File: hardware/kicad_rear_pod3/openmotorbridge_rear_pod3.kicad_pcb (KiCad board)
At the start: 4 copper layers, 50 x 35 mm, 25 parts, among them J1 M8_3PIN_SOCKET, U1 ESP32-C3-WROOM-02, U2 MAX-M10S, U3 SX1262

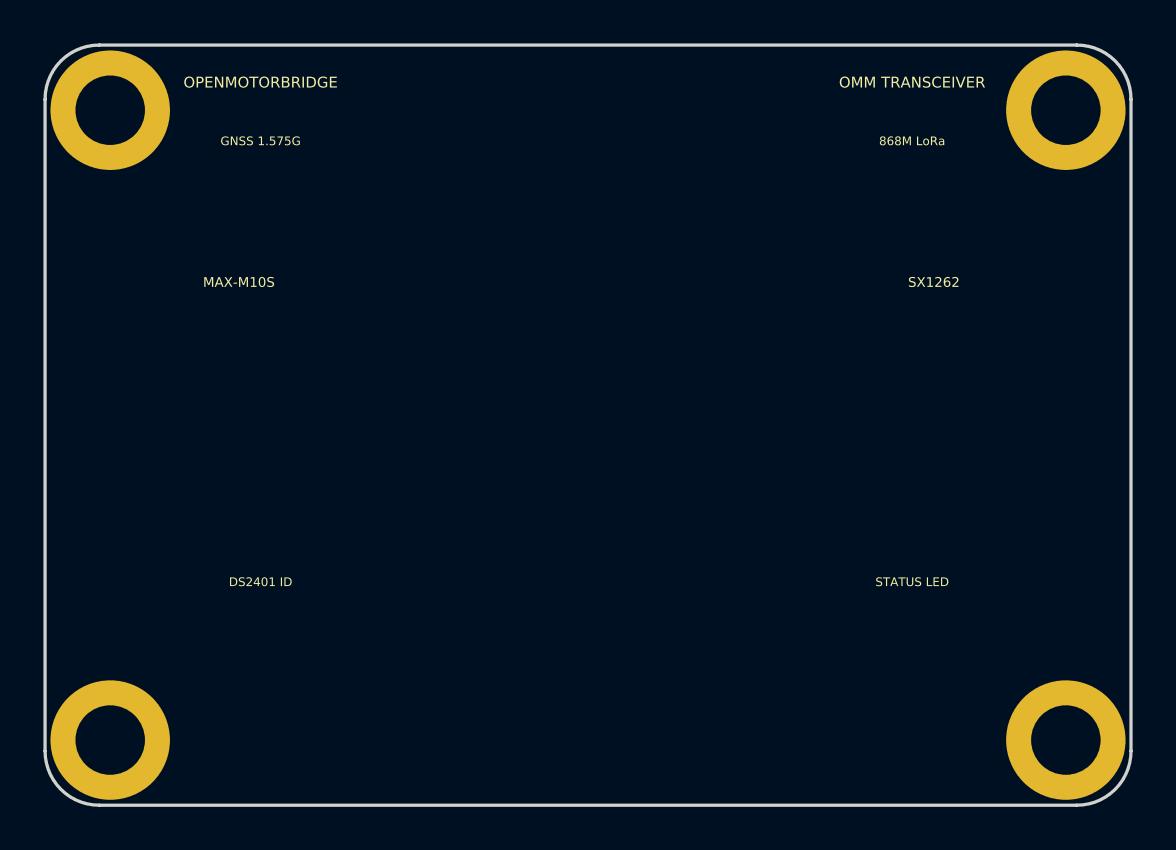
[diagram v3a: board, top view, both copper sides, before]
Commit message: fix(hardware): shift ESP32-C3 module to Y=90.0 on Rear Pod 3 to ensure 2.5mm margin inside PCB outline with zero overhang
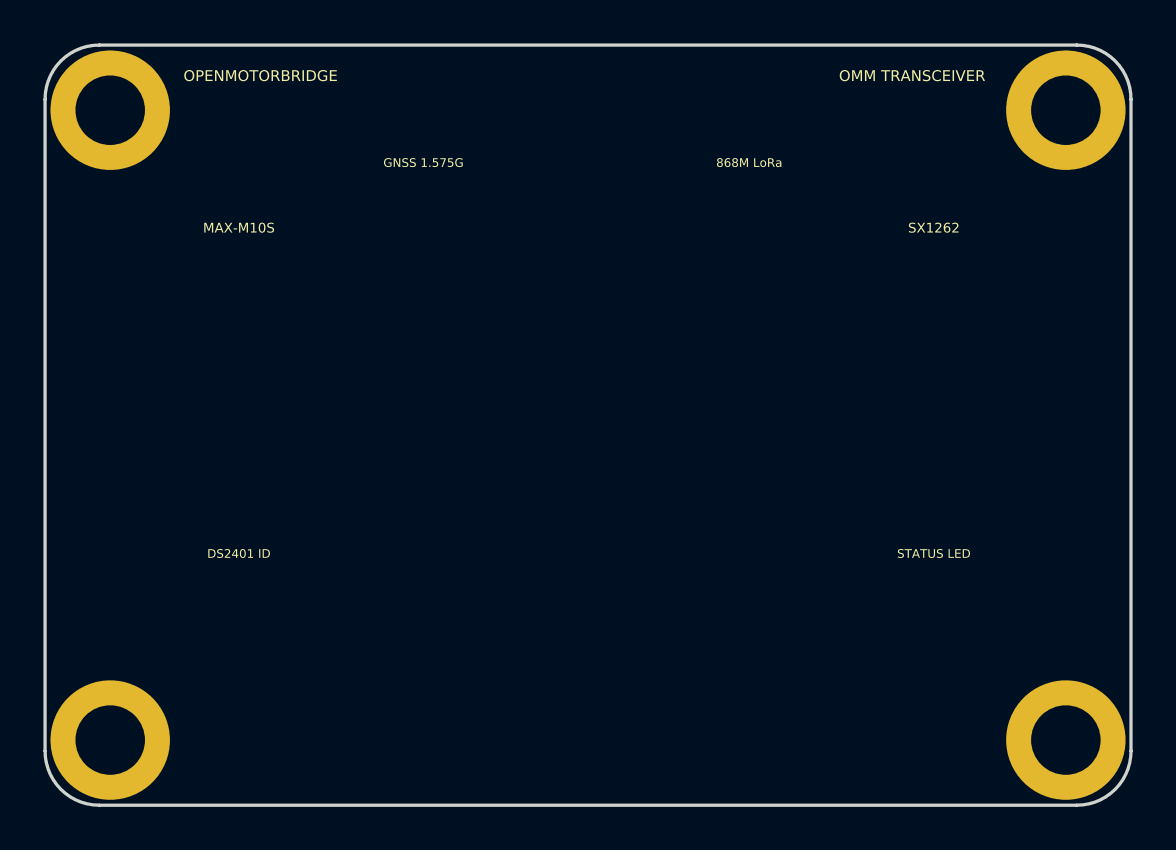
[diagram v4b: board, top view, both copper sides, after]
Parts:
- moved U1 4.00 mm to (125.0, 90.0)
- moved U2 3.00 mm to (109.0, 83.0)
- moved U3 3.00 mm to (141.0, 83.0)
- moved C3 1.50 mm to (109.0, 90.0)
- moved C4 1.50 mm to (145.5, 90.0)
- moved J1 1.50 mm to (125.0, 102.0)
- moved L1 1.50 mm to (141.0, 90.0)
- moved D1 1.41 mm to (141.0, 97.0)
- moved U4 1.41 mm to (109.0, 97.0)
- moved ANT1 1.00 mm to (142.0, 75.0)
- moved ANT2 1.00 mm to (108.0, 75.0)
- moved C1 0.50 mm to (113.5, 93.0)
- moved C2 0.50 mm to (136.5, 93.0)
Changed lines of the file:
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@@
 	(footprint "RF_Module:ESP32-C3-WROOM-02"
 		(layer "F.Cu")
-		(at 125 86)
+		(at 125 90)
 		(property "Reference" "U1"
 			(at 0 -8 0)
@@
 	(footprint ""
 		(layer "F.Cu")
-		(at 141 91.5)
+		(at 141 90)
 		(property "Reference" "L1"
 			(at 0 0 0)
@@
 	(footprint ""
 		(layer "F.Cu")
-		(at 142 76)
+		(at 142 75)
 		(property "Reference" "ANT1"
 			(at 0 0 0)
@@
 	(footprint ""
 		(layer "F.Cu")
-		(at 109 91.5)
+		(at 109 90)
 		(property "Reference" "C3"
 			(at 0 0 0)
@@
 	(footprint "RF_GPS:u-blox_MAX-M10S"
 		(layer "F.Cu")
-		(at 109 86)
+		(at 109 83)
 		(property "Reference" "U2"
 			(at 0 -6 0)
@@
 	(footprint ""
 		(layer "F.Cu")
-		(at 136.5 92.5)
+		(at 136.5 93)
 		(property "Reference" "C2"
 			(at 0 0 0)
@@
 	(footprint ""
 		(layer "F.Cu")
-		(at 110 98)
+		(at 109 97)
 		(property "Reference" "U4"
 			(at 0 0 0)
@@
 	(footprint ""
 		(layer "F.Cu")
-		(at 108 76)
+		(at 108 75)
 		(property "Reference" "ANT2"
 			(at 0 0 0)
@@
 	(footprint ""
 		(layer "F.Cu")
-		(at 140 98)
+		(at 141 97)
 		(property "Reference" "D1"
 			(at 0 0 0)
@@
 	(footprint ""
 		(layer "F.Cu")
-		(at 113.5 92.5)
+		(at 113.5 93)
 		(property "Reference" "C1"
 			(at 0 0 0)
@@
 	(footprint "Package_DFN_QFN:QFN-24-1EP_4x4mm_P0.5mm_EP2.6x2.6mm"
 		(layer "F.Cu")
-		(at 141 86)
+		(at 141 83)
 		(property "Reference" "U3"
 			(at 0 -3.2 0)
@@
 	(footprint ""
 		(layer "F.Cu")
-		(at 145.5 91.5)
+		(at 145.5 90)
 		(property "Reference" "C4"
 			(at 0 0 0)
@@
 	(footprint "Connector_PinHeader_2.54mm:PinHeader_1x03_P2.54mm_Vertical"
 		(layer "B.Cu")
-		(at 125 100.5 90)
+		(at 125 102 90)
 		(property "Reference" "J1"
 			(at 0 -2.5 90)
@@
 		(layer "Edge.Cuts")
 	)
-	(gr_text "GNSS 1.575G"
-		(at 110 74.5 0)
+	(gr_text "DS2401 ID"
+		(at 109 93.5 0)
 		(layer "F.SilkS")
 		(effects
@@
 		)
 	)
-	(gr_text "DS2401 ID"
-		(at 110 94.8 0)
+	(gr_text "GNSS 1.575G"
+		(at 117.5 75.5 0)
 		(layer "F.SilkS")
 		(effects
@@
 	)
 	(gr_text "868M LoRa"
-		(at 140 74.5 0)
+		(at 132.5 75.5 0)
 		(layer "F.SilkS")
 		(effects
@@
 	)
 	(gr_text "STATUS LED"
-		(at 140 94.8 0)
+		(at 141 93.5 0)
 		(layer "F.SilkS")
 		(effects
@@
 	)
 	(gr_text "MAX-M10S"
-		(at 109 81 0)
+		(at 109 78.5 0)
 		(layer "F.SilkS")
 		(effects
@@
 	)
 	(gr_text "SX1262"
-		(at 141 81 0)
+		(at 141 78.5 0)
 		(layer "F.SilkS")
 		(effects
@@
 	)
 	(gr_text "OPENMOTORBRIDGE"
-		(at 110 71.8 0)
+		(at 110 71.5 0)
 		(layer "F.SilkS")
 		(effects
@@
 	)
 	(gr_text "OMM TRANSCEIVER"
-		(at 140 71.8 0)
+		(at 140 71.5 0)
 		(layer "F.SilkS")
 		(effects

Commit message: feat(hardware): implement flat OMM PCB with horizontal front-edge mating, 500mA PTC fuse, and status LED
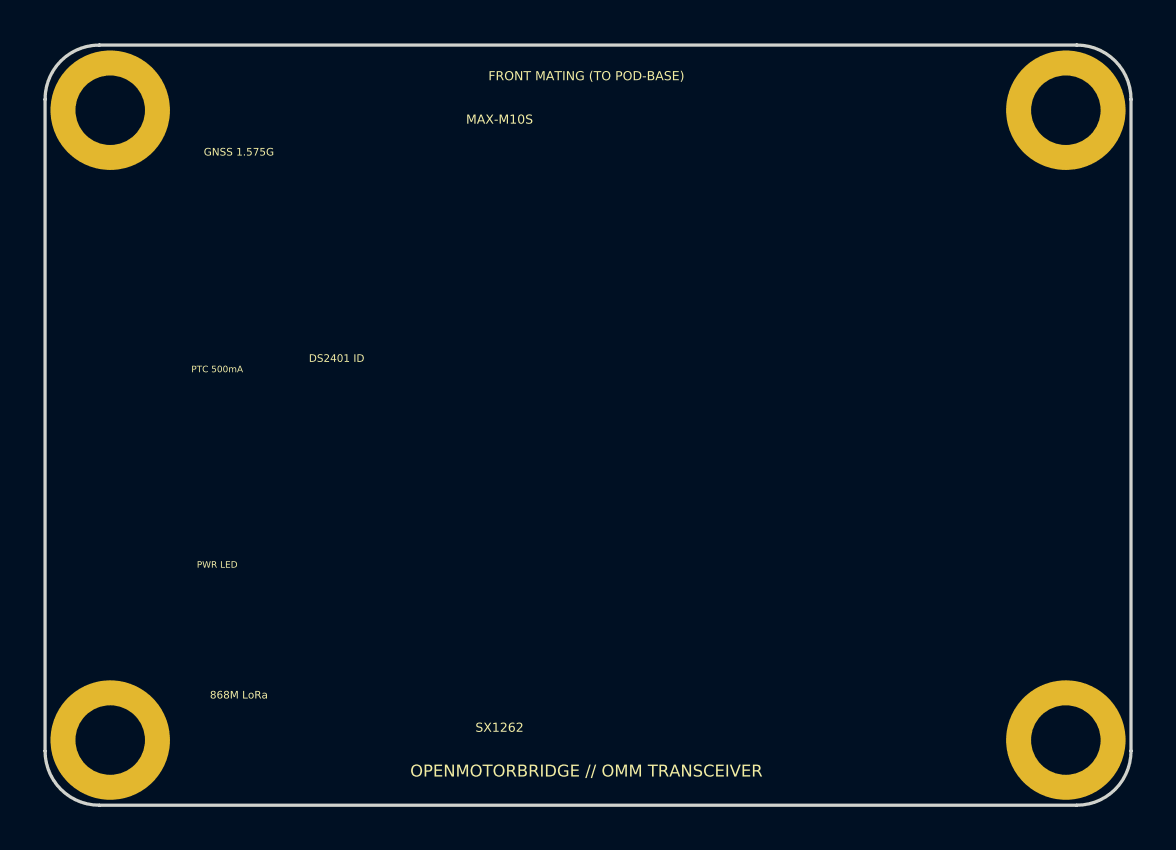
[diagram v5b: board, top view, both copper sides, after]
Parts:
- added F1: , , F.Cu at (108.0, 83.0)
- added R1: , , F.Cu at (108.0, 89.5)
- J1: moved to F.Cu
- moved ANT1 39.7 mm to (109.0, 97.0)
- moved D1 33.4 mm to (108.0, 92.0)
- moved C4 30.6 mm to (116.0, 98.0)
- moved J1 26.8 mm to (102.5, 87.5), turned to 0 degrees
- moved U3 25.0 mm to (121.0, 98.0)
- moved C1 20.2 mm to (129.0, 80.0)
- moved L1 16.1 mm to (127.0, 98.0)
- moved C3 14.8 mm to (116.0, 77.0)
- moved U2 13.4 mm to (121.0, 77.0)
- moved U4 10.5 mm to (113.5, 87.5)
- moved U1 10.0 mm to (135.0, 90.0)
- moved C2 7.76 mm to (129.0, 95.0)
- moved TP1 5.00 mm to (120.0, 78.0)
- moved TP2 5.00 mm to (123.0, 78.0)
- moved TP3 5.00 mm to (137.0, 78.0)
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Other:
- board text added: "FRONT MATING (TO POD-BASE)"
- board text added: "OPENMOTORBRIDGE // OMM TRANSCEIVER"
- board text added: "OPENMOTORBRIDGE // OMM TRANSCEIVER (B.Cu)"
- board text added: "PTC 500mA"
- board text added: "PWR LED"
- board text removed: "6-PIN SOCKET (MATES TO POD-BASE)"
- board text removed: "OMM TRANSCEIVER"
- board text removed: "OPENMOTORBRIDGE"
- board text removed: "STATUS LED"

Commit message: fix(hardware): center horizontal 6-pin socket J1 symmetrically between corner mounting holes H1 and H3
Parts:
- moved J1 6.35 mm to (102.5, 81.2)
- moved R1 1.00 mm to (108.0, 88.5)
- moved D1 0.50 mm to (108.0, 91.5)
- moved F1 0.50 mm to (108.0, 83.5)
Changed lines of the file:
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@@
 	(footprint ""
 		(layer "F.Cu")
-		(at 108 89.5)
+		(at 108 88.5)
 		(property "Reference" "R1"
 			(at 0 0 0)
@@
 	(footprint ""
 		(layer "F.Cu")
-		(at 108 83)
+		(at 108 83.5)
 		(property "Reference" "F1"
 			(at 0 0 0)
@@
 	(footprint ""
 		(layer "F.Cu")
-		(at 108 92)
+		(at 108 91.5)
 		(property "Reference" "D1"
 			(at 0 0 0)
@@
 	(footprint "Connector_PinHeader_2.54mm:PinHeader_1x03_P2.54mm_Vertical"
 		(layer "F.Cu")
-		(at 102.5 87.5)
+		(at 102.5 81.15)
 		(property "Reference" "J1"
 			(at 0 -2.5 0)

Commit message: hardware(rear_pod3): configure 100% integrated antennas (GNSS patch, 868MHz helical coil, 2.4GHz PCB antenna)
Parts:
- moved ANT2 12.2 mm to (121.0, 80.0)
- moved U1 2.69 mm to (136.0, 87.5)
- moved U2 2.00 mm to (121.0, 75.0)
- moved ANT1 1.00 mm to (109.0, 98.0)
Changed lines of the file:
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@@
 	(footprint "RF_Module:ESP32-C3-WROOM-02"
 		(layer "F.Cu")
-		(at 135 90)
+		(at 136 87.5)
 		(property "Reference" "U1"
 			(at 0 -8 0)
@@
 	(footprint ""
 		(layer "F.Cu")
-		(at 109 97)
+		(at 109 98)
 		(property "Reference" "ANT1"
 			(at 0 0 0)
@@
 		(duplicate_pad_numbers_are_jumpers no)
 		(embedded_fonts no)
-		(model "${KICAD10_3DMODEL_DIR}/Connector_Coaxial.3dshapes/U.FL_Hirose_U.FL-R-SMT-1_Vertical.step"
-			(offset
-				(xyz 0 0 0)
-			)
-			(scale
-				(xyz 1 1 1)
+		(model "${KICAD10_3DMODEL_DIR}/Inductor_THT.3dshapes/L_Axial_L11.0mm_D4.5mm_P15.24mm_Horizontal_Fastron_MECC.step"
+			(offset
+				(xyz 0 0 0)
+			)
+			(scale
+				(xyz 0.9 0.9 0.9)
 			)
 			(rotate
@@
 	(footprint "RF_GPS:u-blox_MAX-M10S"
 		(layer "F.Cu")
-		(at 121 77)
+		(at 121 75)
 		(property "Reference" "U2"
 			(at 0 -6 0)
@@
 	(footprint ""
 		(layer "F.Cu")
-		(at 109 78)
+		(at 121 80)
 		(property "Reference" "ANT2"
 			(at 0 0 0)
@@
 		(duplicate_pad_numbers_are_jumpers no)
 		(embedded_fonts no)
-		(model "${KICAD10_3DMODEL_DIR}/Connector_Coaxial.3dshapes/U.FL_Hirose_U.FL-R-SMT-1_Vertical.step"
-			(offset
-				(xyz 0 0 0)
-			)
-			(scale
-				(xyz 1 1 1)
-			)
-			(rotate
+		(model "${KICAD10_3DMODEL_DIR}/RF_Antenna.3dshapes/Pulse_W3000.step"
+			(offset
+				(xyz 0 0 0)
+			)
+			(scale
+				(xyz 1.8 1.8 1.5)
+			)
+			(rotate

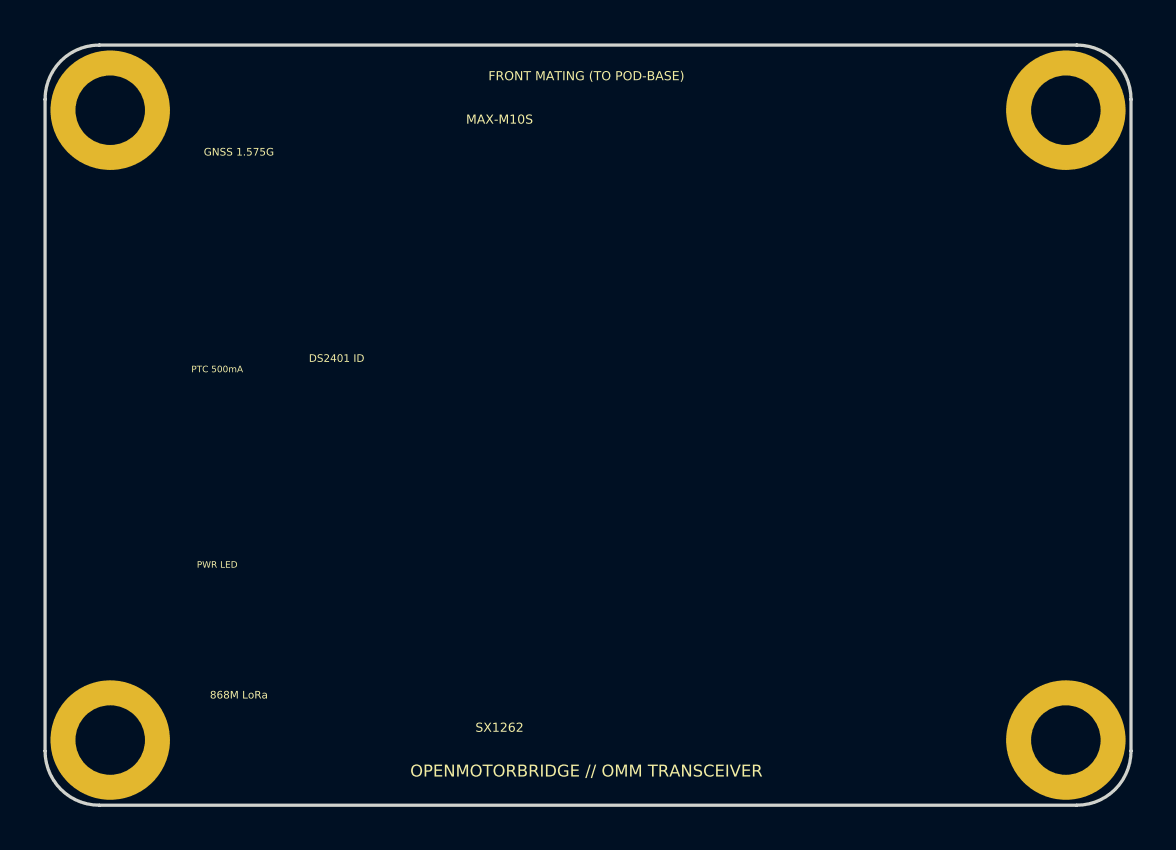
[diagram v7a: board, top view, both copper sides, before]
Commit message: hardware(rear_pod3): resolve all component collisions with quadrant-isolated HF zoning
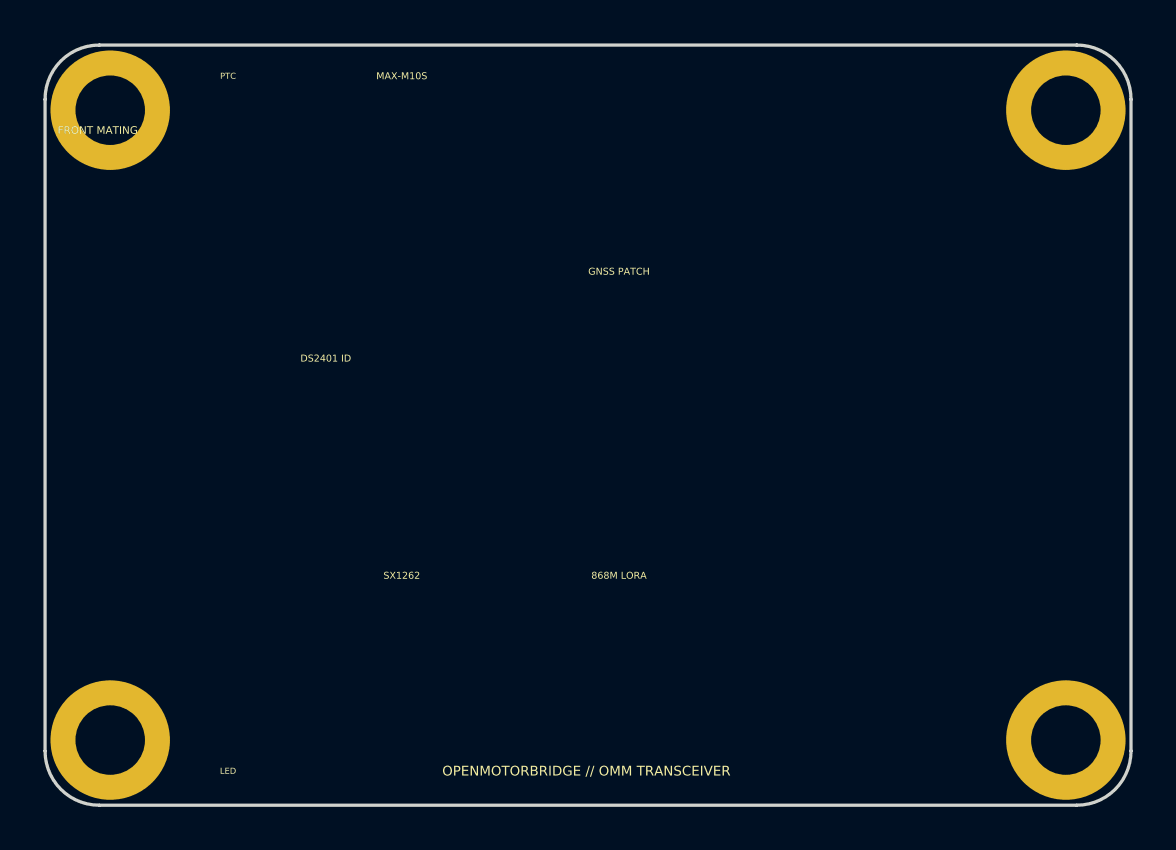
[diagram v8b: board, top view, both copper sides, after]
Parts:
- moved ANT1 17.6 mm to (126.5, 100.0)
- moved L1 15.1 mm to (112.0, 100.0)
- moved TP3 14.5 mm to (126.0, 87.5)
- moved TP4 14.5 mm to (129.0, 87.5)
- moved TP1 9.50 mm to (120.0, 87.5)
- moved TP2 9.50 mm to (123.0, 87.5)
- moved D1 9.01 mm to (108.5, 100.5)
- moved F1 9.01 mm to (108.5, 74.5)
- moved R1 9.01 mm to (108.5, 97.5)
- moved ANT2 7.43 mm to (126.5, 75.0)
- moved C1 7.11 mm to (134.5, 84.5)
- moved C2 7.11 mm to (134.5, 90.5)
- moved C4 6.40 mm to (112.0, 103.0)
- moved U1 6.00 mm to (142.0, 87.5)
- moved U3 4.92 mm to (116.5, 100.0)
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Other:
- board text added: "868M LORA"
- board text added: "FRONT MATING"
- board text added: "GNSS PATCH"
- board text added: "LED"
- board text added: "PTC"
- board text removed: "868M LoRa"
- board text removed: "FRONT MATING (TO POD-BASE)"
- board text removed: "GNSS 1.575G"
- board text removed: "PTC 500mA"
- board text removed: "PWR LED"
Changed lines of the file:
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@@
 	(footprint "RF_Module:ESP32-C3-WROOM-02"
 		(layer "F.Cu")
-		(at 136 87.5)
+		(at 142 87.5)
 		(property "Reference" "U1"
 			(at 0 -8 0)
@@
 	(footprint ""
 		(layer "F.Cu")
-		(at 127 98)
+		(at 112 100)
 		(property "Reference" "L1"
 			(at 0 0 0)
@@
 	(footprint ""
 		(layer "F.Cu")
-		(at 108 88.5)
+		(at 108.5 97.5)
 		(property "Reference" "R1"
 			(at 0 0 0)
@@
 	(footprint ""
 		(layer "F.Cu")
-		(at 109 98)
+		(at 126.5 100)
 		(property "Reference" "ANT1"
 			(at 0 0 0)
@@
 			)
 			(scale
-				(xyz 0.9 0.9 0.9)
-			)
-			(rotate
-				(xyz 0 0 0)
-			)
-		)
-	)
-	(footprint ""
-		(layer "F.Cu")
-		(at 116 77)
+				(xyz 0.6 0.6 0.6)
+			)
+			(rotate
+				(xyz 0 0 0)
+			)
+		)
+	)
+	(footprint ""
+		(layer "F.Cu")
+		(at 112 75)
 		(property "Reference" "C3"
 			(at 0 0 0)
@@
 	(footprint "RF_GPS:u-blox_MAX-M10S"
 		(layer "F.Cu")
-		(at 121 75)
+		(at 116.5 75)
 		(property "Reference" "U2"
 			(at 0 -6 0)
@@
 	(footprint ""
 		(layer "F.Cu")
-		(at 129 95)
+		(at 134.5 90.5)
 		(property "Reference" "C2"
 			(at 0 0 0)
@@
 	(footprint ""
 		(layer "F.Cu")
-		(at 113.5 87.5)
+		(at 113 87.5)
 		(property "Reference" "U4"
 			(at 0 0 0)
@@
 	(footprint ""
 		(layer "F.Cu")
-		(at 121 80)
+		(at 126.5 75)
 		(property "Reference" "ANT2"
 			(at 0 0 0)
@@
 			)
 			(scale
-				(xyz 1.8 1.8 1.5)
+				(xyz 0.9 0.9 1)
 			)
 			(rotate
@@
 	(footprint ""
 		(layer "F.Cu")
-		(at 108 83.5)
+		(at 108.5 74.5)
 		(property "Reference" "F1"
 			(at 0 0 0)
@@
 	(footprint ""
 		(layer "F.Cu")
-		(at 108 91.5)
+		(at 108.5 100.5)
 		(property "Reference" "D1"
 			(at 0 0 0)
@@
 	(footprint ""
 		(layer "F.Cu")
-		(at 129 80)
+		(at 134.5 84.5)
 		(property "Reference" "C1"
 			(at 0 0 0)
@@
 	(footprint "Package_DFN_QFN:QFN-24-1EP_4x4mm_P0.5mm_EP2.6x2.6mm"
 		(layer "F.Cu")
-		(at 121 98)
+		(at 116.5 100)
 		(property "Reference" "U3"
 			(at 0 -3.2 0)
@@
 	(footprint ""
 		(layer "F.Cu")
-		(at 116 98)
+		(at 112 103)
 		(property "Reference" "C4"
 			(at 0 0 0)
@@
 	(footprint ""
 		(layer "B.Cu")
-		(at 140 78)
+		(at 129 87.5)
 		(property "Reference" "TP4"
 			(at 0 0 0)
@@
 	(footprint ""
 		(layer "B.Cu")
-		(at 137 78)
+		(at 126 87.5)
 		(property "Reference" "TP3"
 			(at 0 0 0)
@@
 	(footprint ""
 		(layer "B.Cu")
-		(at 123 78)
+		(at 123 87.5)
 		(property "Reference" "TP2"
 			(at 0 0 0)
@@
 	(footprint ""
 		(layer "B.Cu")
-		(at 120 78)
+		(at 120 87.5)
 		(property "Reference" "TP1"
 			(at 0 0 0)
@@
 		(layer "Edge.Cuts")
 	)
-	(gr_text "PTC 500mA"
-		(at 108 85 0)
+	(gr_text "PTC"
+		(at 108.5 71.5 0)
 		(layer "F.SilkS")
 		(effects
 			(font
-				(size 0.3 0.3)
-				(thickness 0.07)
-			)
-		)
-	)
-	(gr_text "PWR LED"
-		(at 108 94 0)
+				(size 0.28 0.28)
+				(thickness 0.06)
+			)
+		)
+	)
+	(gr_text "LED"
+		(at 108.5 103.5 0)
 		(layer "F.SilkS")
 		(effects
 			(font
-				(size 0.3 0.3)
+				(size 0.28 0.28)
+				(thickness 0.06)
+			)
+		)
+	)
+	(gr_text "DS2401 ID"
+		(at 113 84.5 0)
+		(layer "F.SilkS")
+		(effects
+			(font
+				(size 0.32 0.32)
 				(thickness 0.07)
 			)
 		)
 	)
-	(gr_text "GNSS 1.575G"
-		(at 109 75 0)
+	(gr_text "MAX-M10S"
+		(at 116.5 71.5 0)
+		(layer "F.SilkS")
+		(effects
+			(font
+				(size 0.32 0.32)
+				(thickness 0.07)
+			)
+		)
+	)
+	(gr_text "SX1262"
+		(at 116.5 94.5 0)
+		(layer "F.SilkS")
+		(effects
+			(font
+				(size 0.32 0.32)
+				(thickness 0.07)
+			)
+		)
+	)
+	(gr_text "GNSS PATCH"
+		(at 126.5 80.5 0)
+		(layer "F.SilkS")
+		(effects
+			(font
+				(size 0.32 0.32)
+				(thickness 0.07)
+			)
+		)
+	)
+	(gr_text "868M LORA"
+		(at 126.5 94.5 0)
+		(layer "F.SilkS")
+		(effects
+			(font
+				(size 0.32 0.32)
+				(thickness 0.07)
+			)
+		)
+	)
+	(gr_text "FRONT MATING"
+		(at 102.5 74 0)
 		(layer "F.SilkS")
 		(effects
@@
 		)
 	)
-	(gr_text "868M LoRa"
-		(at 109 100 0)
-		(layer "F.SilkS")
-		(effects
-			(font
-				(size 0.35 0.35)
-				(thickness 0.08)
-			)
-		)
-	)
-	(gr_text "DS2401 ID"
-		(at 113.5 84.5 0)
-		(layer "F.SilkS")
-		(effects
-			(font
-				(size 0.35 0.35)
-				(thickness 0.08)
-			)
-		)
-	)
-	(gr_text "MAX-M10S"
-		(at 121 73.5 0)
-		(layer "F.SilkS")
-		(effects
-			(font
-				(size 0.42 0.42)
-				(thickness 0.09)
-			)
-		)
-	)
-	(gr_text "SX1262"
-		(at 121 101.5 0)
-		(layer "F.SilkS")
-		(effects
-			(font
-				(size 0.42 0.42)
-				(thickness 0.09)
-			)
-		)
-	)
-	(gr_text "FRONT MATING (TO POD-BASE)"
-		(at 125 71.5 0)
-		(layer "F.SilkS")
-		(effects
-			(font
-				(size 0.42 0.42)
-				(thickness 0.1)
-			)
-		)
-	)
 	(gr_text "OPENMOTORBRIDGE // OMM TRANSCEIVER"
 		(at 125 103.5 0)
@@
 		(effects
 			(font
-				(size 0.55 0.55)
-				(thickness 0.12)
-			)
-		)
+				(size 0.45 0.45)
+				(thickness 0.09)
+			)
+		)
